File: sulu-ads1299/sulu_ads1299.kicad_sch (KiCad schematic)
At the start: 19 parts

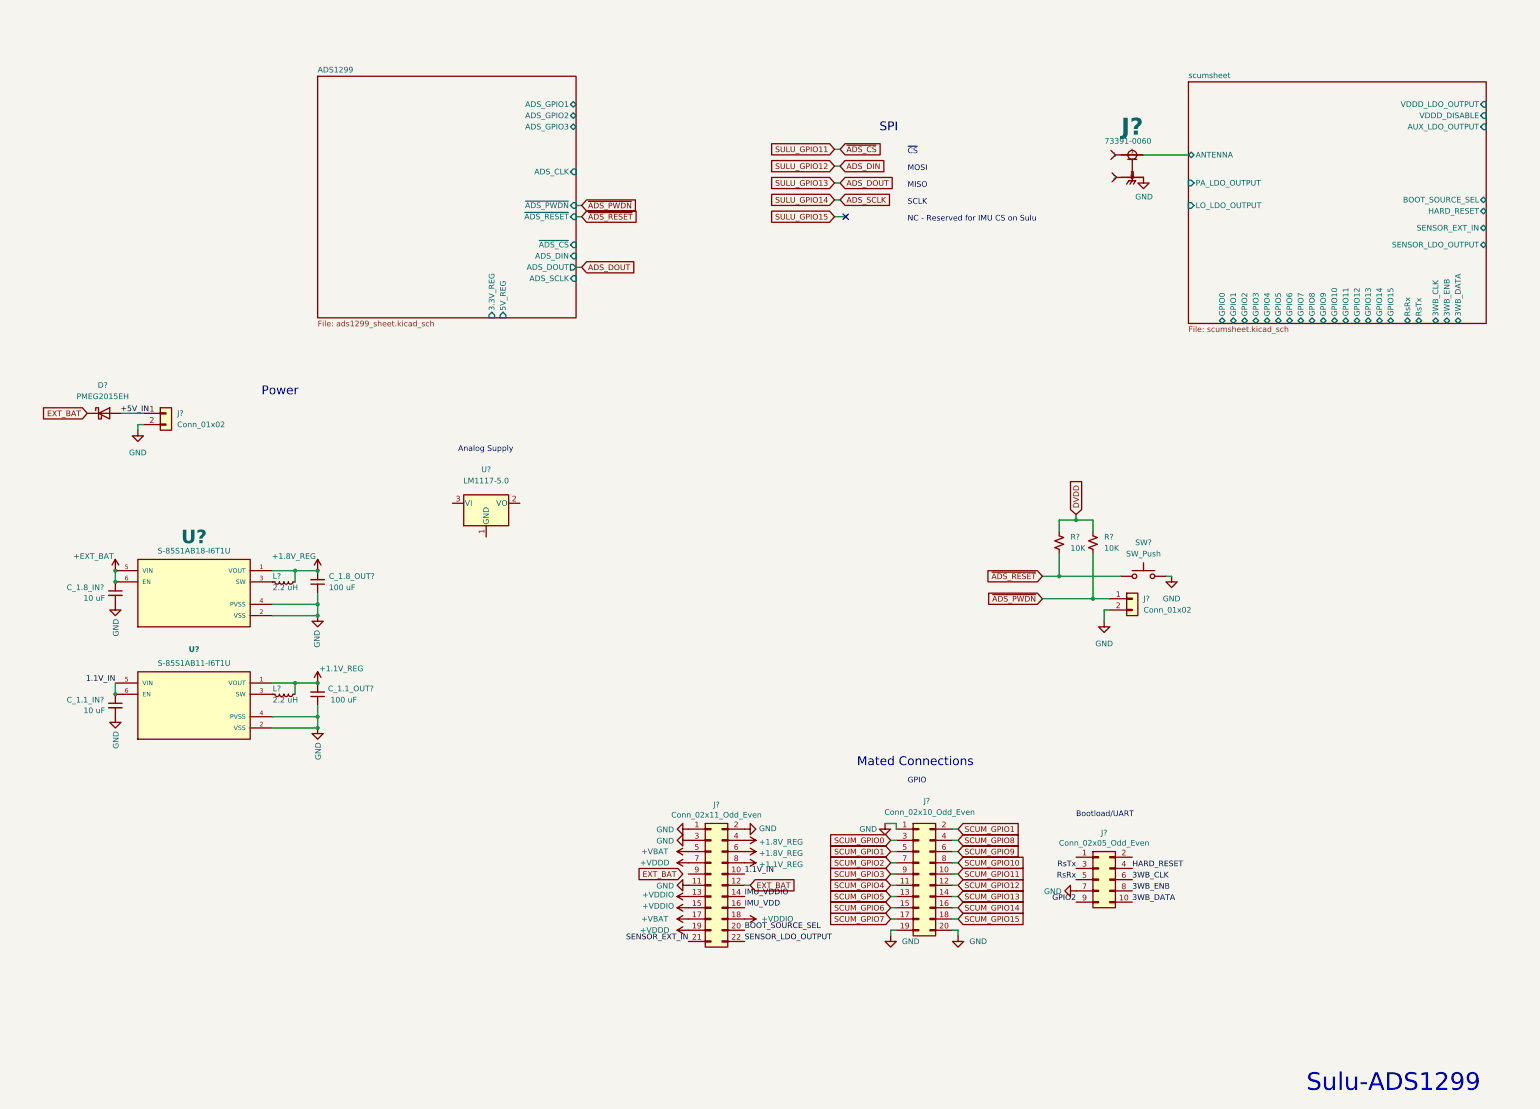
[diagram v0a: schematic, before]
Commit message: Sulu-ads1299 schematic largely completed
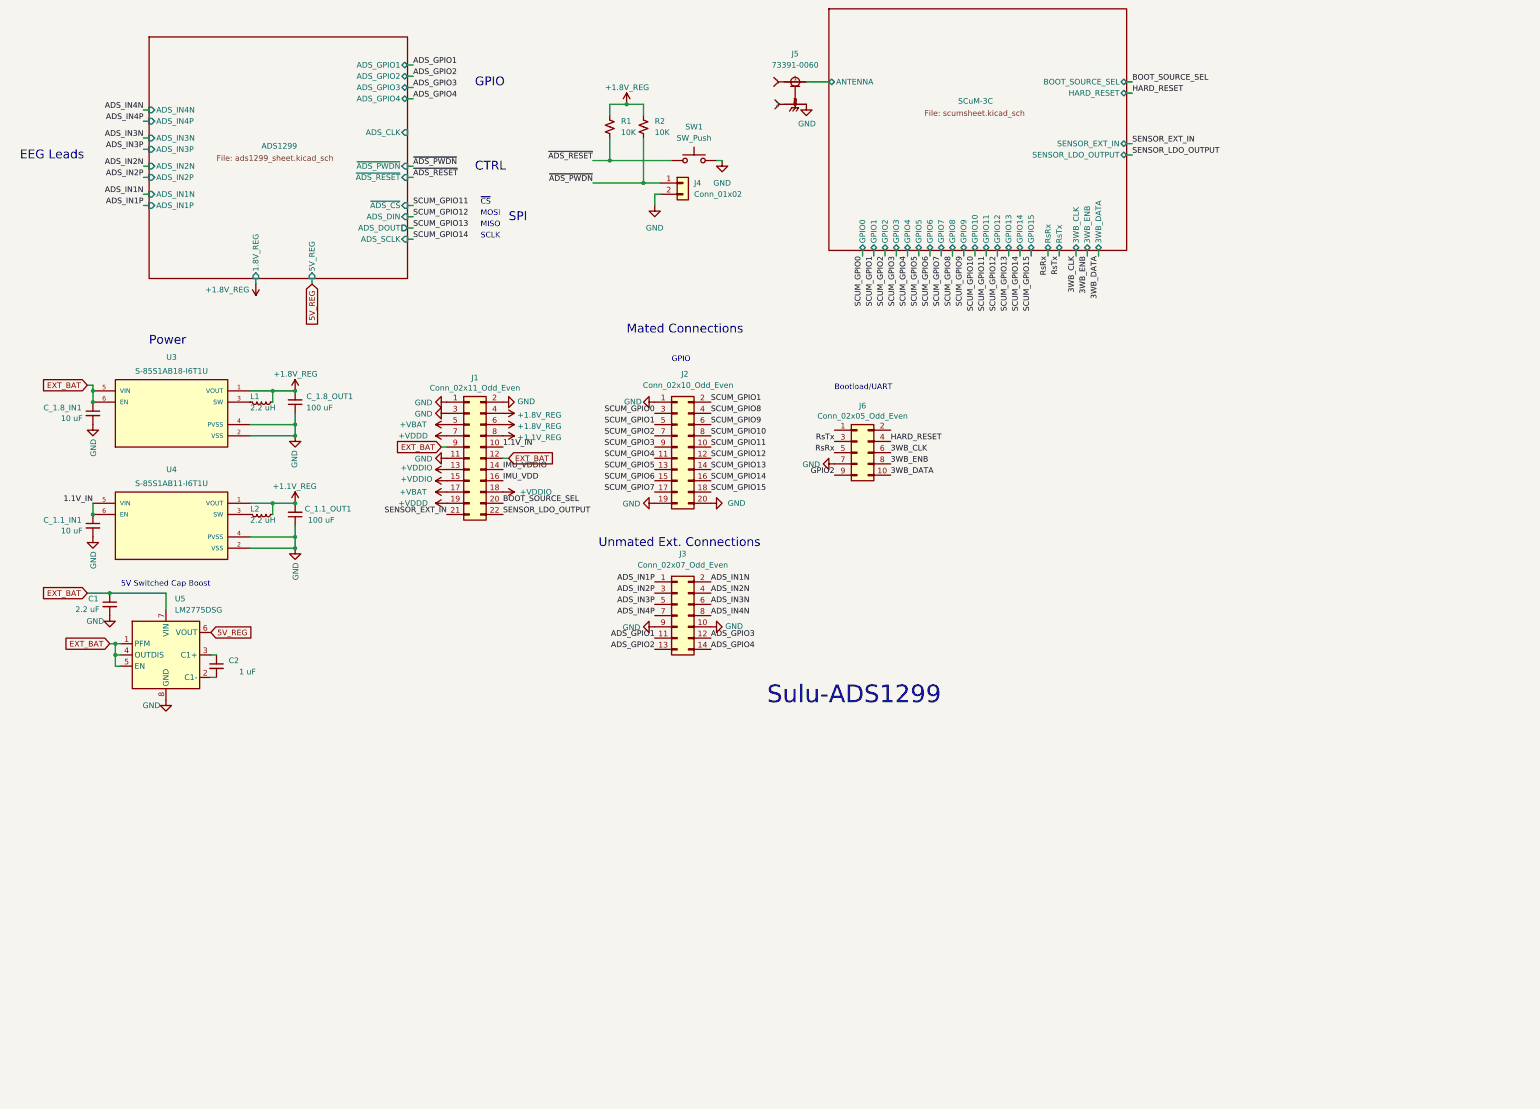
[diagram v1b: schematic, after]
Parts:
- removed D?: PMEG2015EH, Diode_SMD:D_SOD-123F, symbol Diode:PMEG2015EH
- removed J?: Conn_01x02, symbol Connector_Generic:Conn_01x02
- removed U?: LM1117-5.0, symbol Regulator_Linear:LM1117-5.0
- added C1: 2.2 uF, Capacitor_SMD:C_0402_1005Metric, symbol Device:C_Small
- added C2: 1 uF, Capacitor_SMD:C_0402_1005Metric, symbol Device:C_Small
- added J3: Conn_02x07_Odd_Even, symbol Connector_Generic:Conn_02x07_Odd_Even
- added U5: LM2775DSG, Package_SON:WSON-8-1EP_2x2mm_P0.5mm_EP0.9x1.6mm_ThermalVias, symbol Regulator_SwitchedCapacitor:LM2775DSG
- gave numbers to parts that had none: 16
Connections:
- net +EXT_BAT is gone; now on net EXT_BAT: C_1.8_IN1.1, U3.5 (VIN), U3.6 (EN)
- net DVDD is gone; now on net +1.8V_REG: R1.1, R2.1
- net EXT_BAT: now also J1.9 (Pin_9), C1.1, U5.1 (PFM), U5.4 (OUTDIS), U5.5 (EN), U5.7 (VIN)
- net GND: now also C1.2, J3.10 (Pin_10), J3.9 (Pin_9), U5.8 (GND), U5.9 (GND)
- new net: C2.1, U5.3 (C1+)
- new net: C2.2, U5.2 (C1-)
- new net 5V_REG: U5.6 (VOUT)
- new net ADS_GPIO1: J3.11 (Pin_11)
- new net ADS_GPIO2: J3.13 (Pin_13)
- new net ADS_GPIO3: J3.12 (Pin_12)
- new net ADS_GPIO4: J3.14 (Pin_14)
- new net ADS_IN1N: J3.2 (Pin_2)
- new net ADS_IN1P: J3.1 (Pin_1)
- new net ADS_IN2N: J3.4 (Pin_4)
- new net ADS_IN2P: J3.3 (Pin_3)
- new net ADS_IN3N: J3.6 (Pin_6)
- new net ADS_IN3P: J3.5 (Pin_5)
- new net ADS_IN4N: J3.8 (Pin_8)
- new net ADS_IN4P: J3.7 (Pin_7)
- no-connect marks 1 -> 0
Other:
- sheet scumsheet renamed SCuM-3C
- sheet ADS1299 ports: added 1.8V_REG, ADS_GPIO4, ADS_IN1N, ADS_IN1P, ADS_IN2N, ADS_IN2P, ADS_IN3N, ADS_IN3P, ADS_IN4N, ADS_IN4P; removed 3.3V_REG
- sheet SCuM-3C ports: added none; removed AUX_LDO_OUTPUT, LO_LDO_OUTPUT, PA_LDO_OUTPUT, VDDD_DISABLE, VDDD_LDO_OUTPUT
- note added: "5V Switched Cap Boost"
- note added: "CTRL"
- note added: "EEG Leads"
- note added: "Unmated Ext. Connections"
- note removed: "Analog Supply"
- note removed: "NC - Reserved for IMU CS on Sulu"
- moved on the sheet: C_1.1_IN1, C_1.1_OUT1, C_1.8_IN1, C_1.8_OUT1, J1, J2, J4, J5, J6, L1, L2, R1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

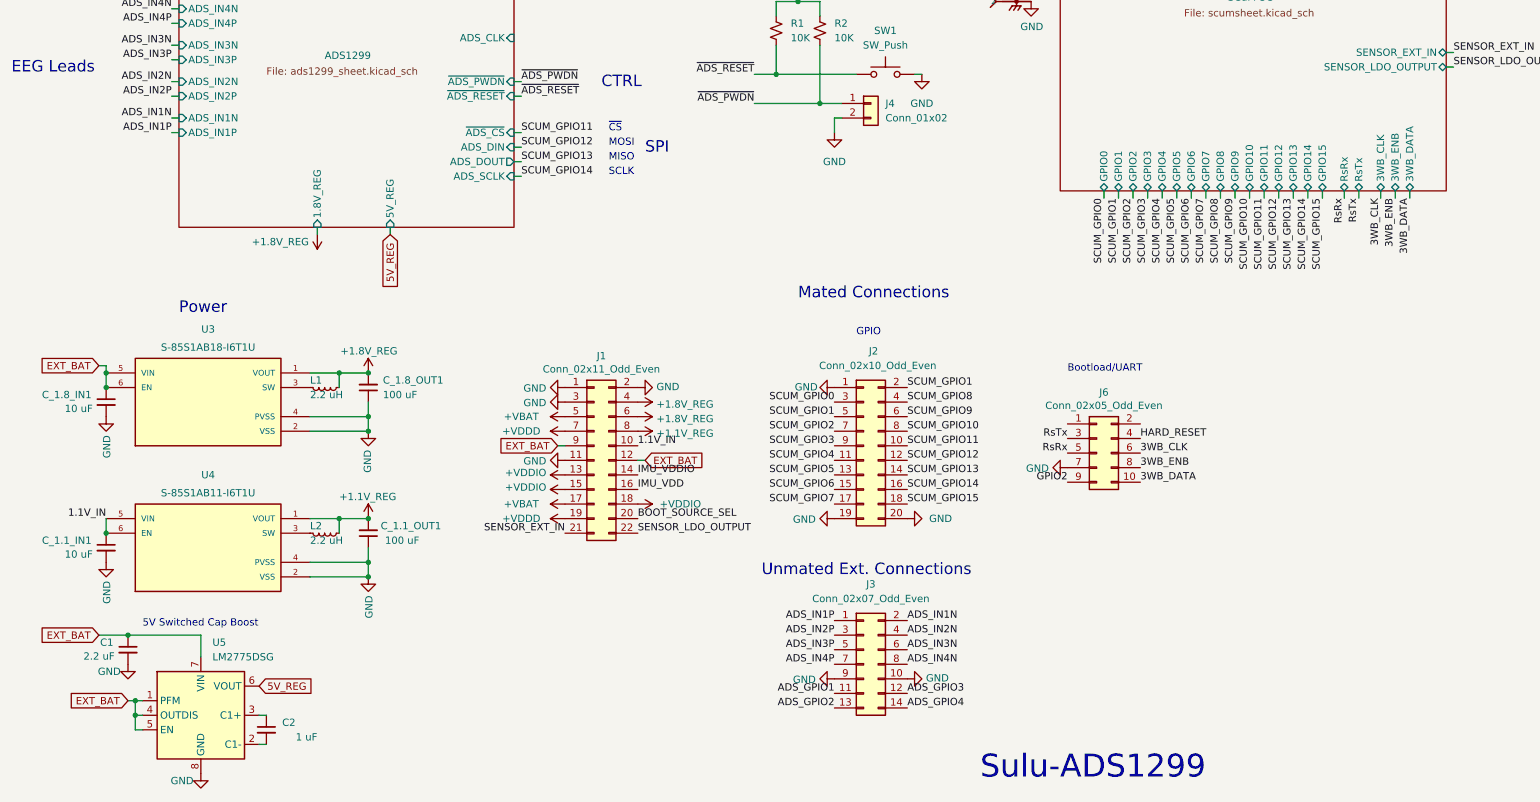
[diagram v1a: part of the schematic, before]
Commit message: Sulu-ads1299 migrating libs and fixing ERC
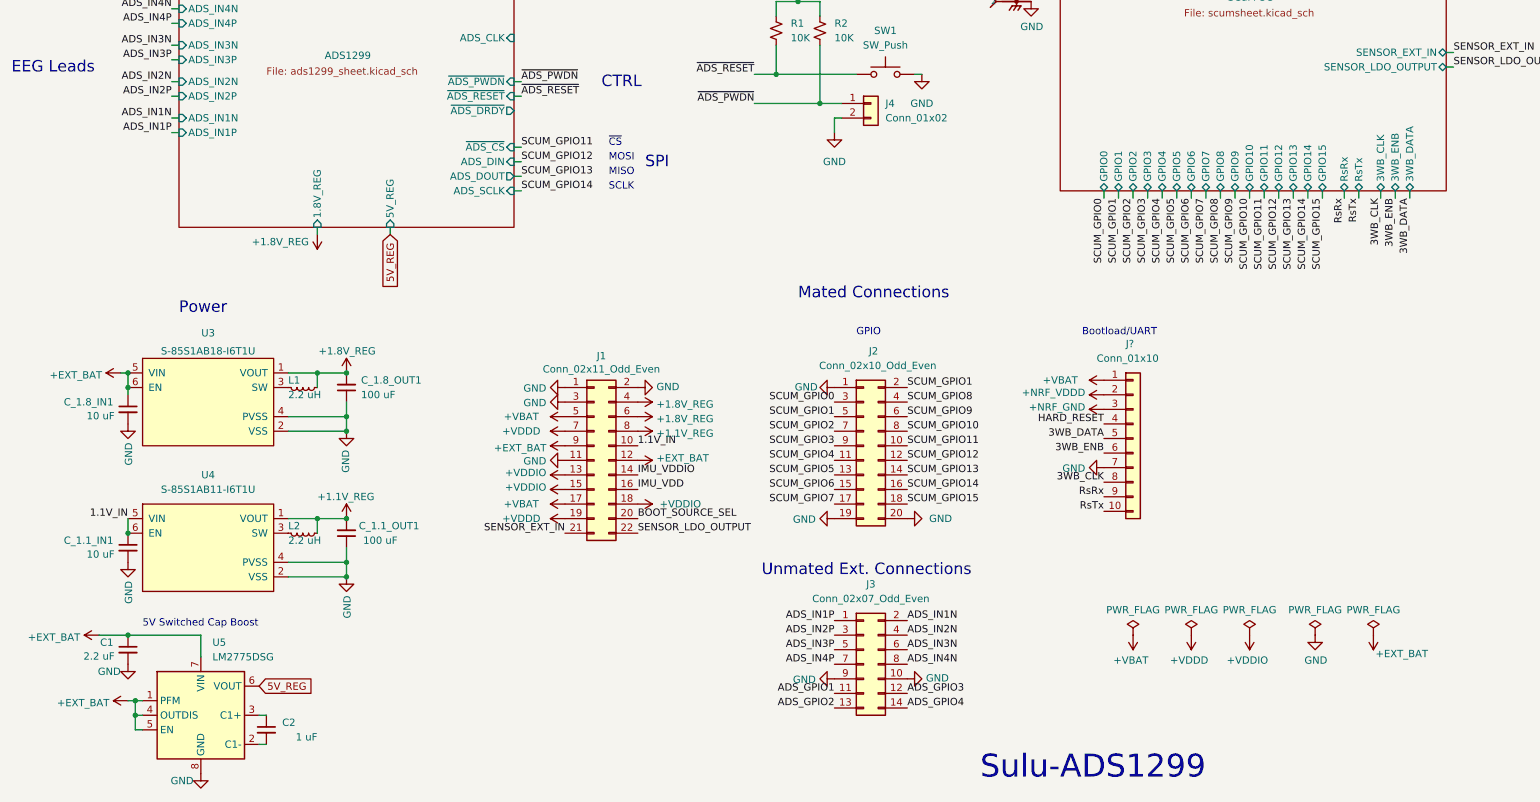
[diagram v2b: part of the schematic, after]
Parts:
- removed J6: Conn_02x05_Odd_Even, Connector_PinHeader_2.54mm:PinHeader_2x05_P2.54mm_Vertical, symbol Connector_Generic:Conn_02x05_Odd_Even
- added J?: Conn_01x10, Connector_PinHeader_2.54mm:PinHeader_1x10_P2.54mm_Vertical, symbol Connector_Generic:Conn_01x10
- J5: symbol 73391-0060:73391-0060 -> draft1library:73391-0060
- U3: symbol S-85S1AB20-I6T1U:S-85S1AB18-I6T1U -> draft1library:S-85S1AB18-I6T1U
- U4: symbol S-85S1AB20-I6T1U:S-85S1AB11-I6T1U -> draft1library:S-85S1AB11-I6T1U
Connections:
- net +VBAT: now also J?.1 (Pin_1)
- net 3WB_CLK: now also J?.8 (Pin_8)
- net 3WB_DATA: now also J?.5 (Pin_5)
- net 3WB_ENB: now also J?.6 (Pin_6)
- net GND: now also J?.7 (Pin_7)
- net HARD_RESET: now also J?.4 (Pin_4)
- net RsRx: now also J?.9 (Pin_9)
- net RsTx: now also J?.10 (Pin_10)
- net EXT_BAT renamed +EXT_BAT
- new net +NRF_GND: J?.3 (Pin_3)
- new net +NRF_VDDD: J?.2 (Pin_2)
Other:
- sheet ADS1299 ports: added ~{ADS_DRDY}; removed none
- moved on the sheet: C_1.1_IN1, C_1.1_OUT1, C_1.8_IN1, C_1.8_OUT1, L1, L2

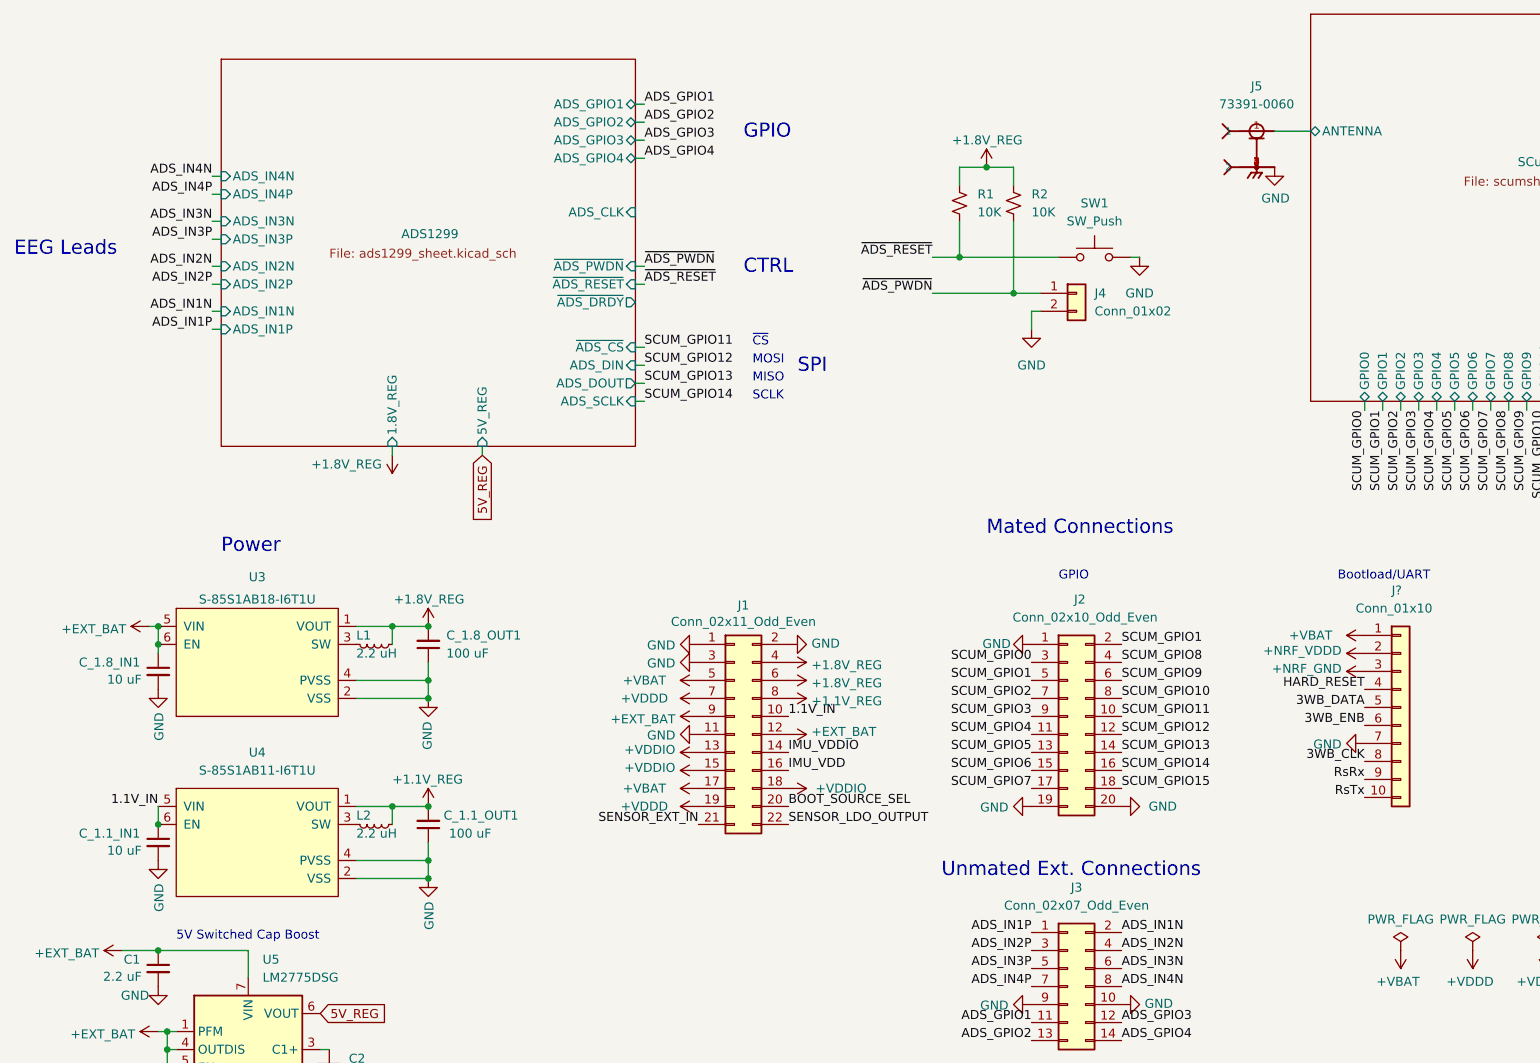
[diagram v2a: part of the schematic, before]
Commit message: Sulu-ads1299 started layout & imported shared footprints
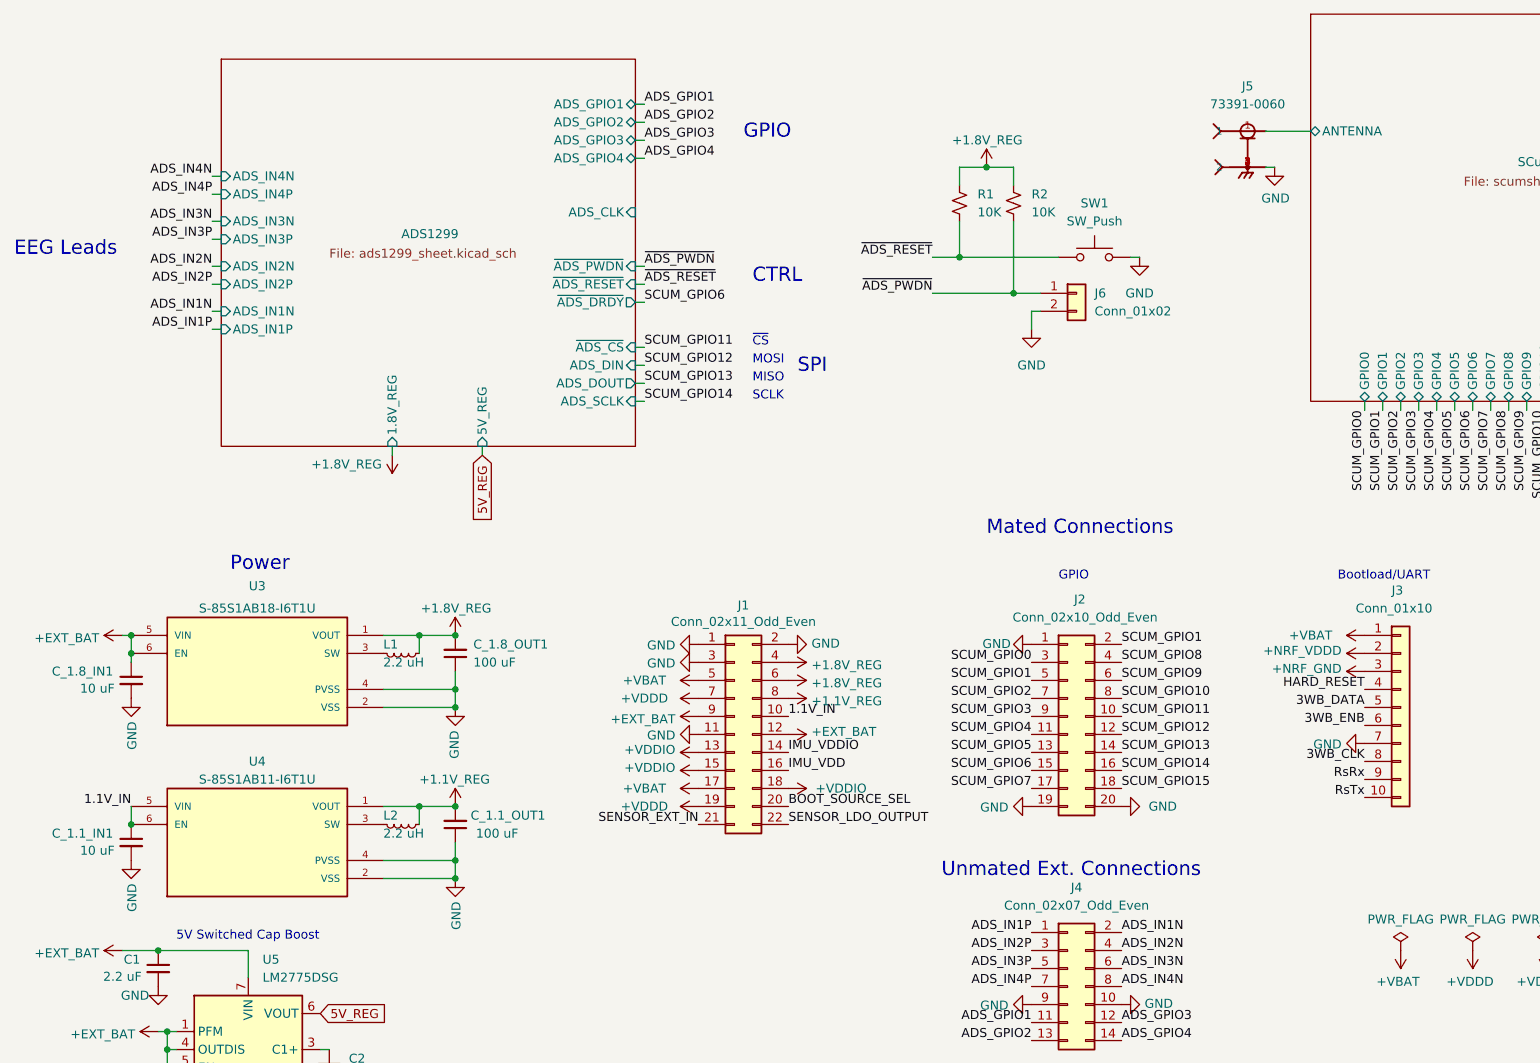
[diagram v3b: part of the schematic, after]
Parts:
- J4: renamed from J3; footprint (none) -> Connector_PinHeader_2.54mm:PinHeader_2x07_P2.54mm_Vertical
- J5: symbol draft1library:73391-0060 -> 73391-0060:73391-0060
- J6: renamed from J4; footprint (none) -> Connector_PinHeader_2.54mm:PinHeader_1x02_P2.54mm_Vertical
- R1, R2: footprint (none) -> Resistor_SMD:R_0402_1005Metric
- U3: symbol draft1library:S-85S1AB18-I6T1U -> S-85S1AB20-I6T1U:S-85S1AB18-I6T1U
- U4: symbol draft1library:S-85S1AB11-I6T1U -> S-85S1AB20-I6T1U:S-85S1AB11-I6T1U
- gave numbers to parts that had none: 1
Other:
- moved on the sheet: C_1.1_IN1, C_1.1_OUT1, C_1.8_IN1, C_1.8_OUT1, J5, L1, L2, U3
